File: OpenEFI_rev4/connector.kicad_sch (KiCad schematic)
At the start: 58 parts, among them J6 1241434-1, Q10 PMN30XPX, Q20 PMN30XPX, Q5 SS8050, Q6 IRLZ44N, Q7 IRLZ44N, U14 MIC5205-3.3YM5, U16 TPS5430DDA, U17 L78M05ABDT-TR, U4 AMS1117-3.3, U6 LT4363IMS

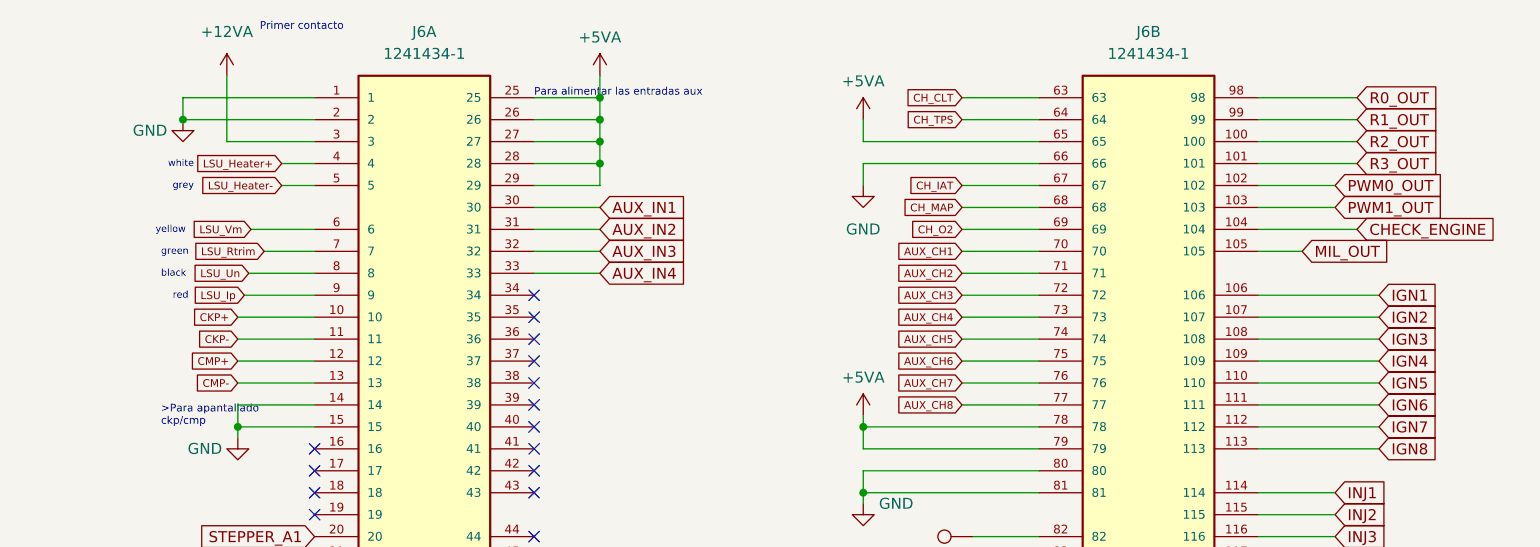
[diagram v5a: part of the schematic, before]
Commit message: fix board errors
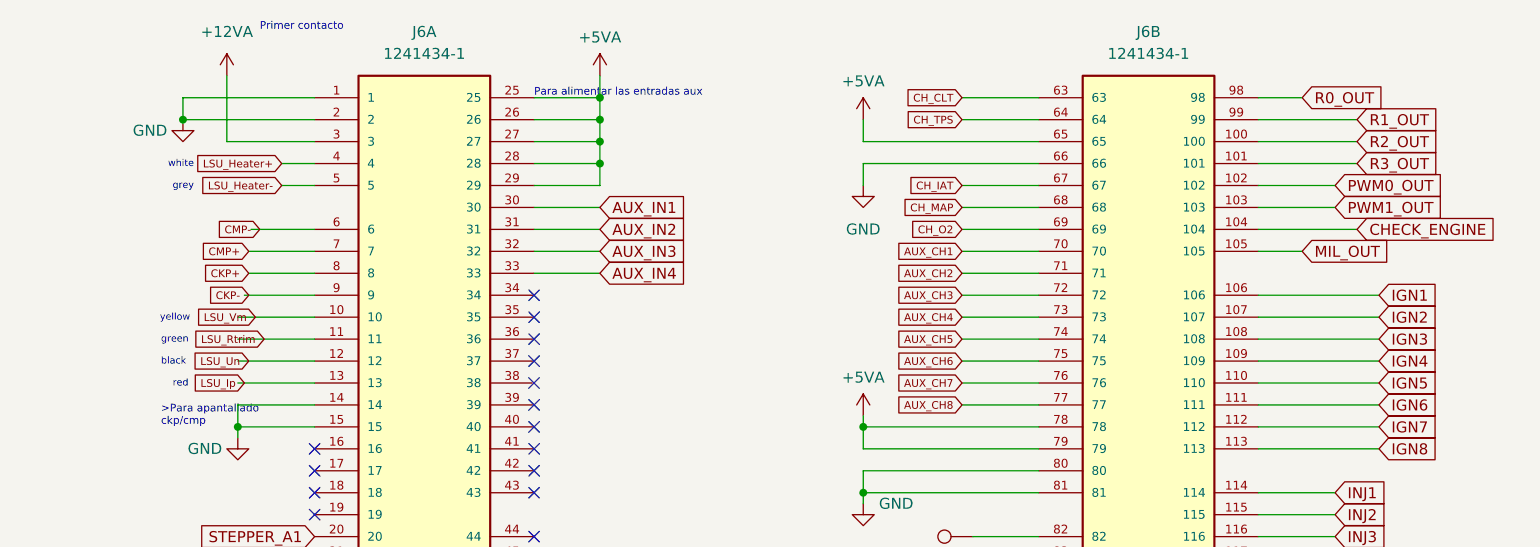
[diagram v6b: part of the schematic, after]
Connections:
- net CKP+: now also J6.8; no longer J6.10
- net CKP-: now also J6.9; no longer J6.11
- net CMP+: now also J6.7; no longer J6.12
- net CMP-: now also J6.6; no longer J6.13
- net LSU_Ip: now also J6.13; no longer J6.9
- net LSU_Rtrim: now also J6.11; no longer J6.7
- net LSU_Un: now also J6.12; no longer J6.8
- net LSU_Vm: now also J6.10; no longer J6.6
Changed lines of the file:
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@@
     (stroke (width 0) (type default))
   )
-  (wire (pts (xy 256.54 27.94) (xy 267.97 27.94))
+  (wire (pts (xy 256.54 27.94) (xy 261.62 27.94))
     (stroke (width 0) (type default))
   )
@@
     (stroke (width 0) (type default))
   )
-  (wire (pts (xy 141.478 45.72) (xy 147.32 45.72))
+  (wire (pts (xy 139.7 45.72) (xy 147.32 45.72))
     (stroke (width 0) (type default))
   )
@@
     (fill (type none))
   )
-  (text "yellow" (at 128.905 43.815 0)
+  (text "yellow" (at 129.413 53.975 0)
     (effects (font (size 0.8 0.8)) (justify left bottom))
   )
@@
     (effects (font (size 0.889 0.889)) (justify left bottom))
   )
-  (text "green" (at 129.54 46.355 0)
+  (text "green" (at 129.54 56.515 0)
     (effects (font (size 0.8 0.8)) (justify left bottom))
   )
@@
     (effects (font (size 0.8 0.8)) (justify right bottom))
   )
-  (text "black" (at 129.54 48.895 0)
+  (text "black" (at 129.54 59.055 0)
     (effects (font (size 0.8 0.8)) (justify left bottom))
   )
@@
     (effects (font (size 2 2)) (justify left bottom))
   )
-  (text "red" (at 132.715 51.435 0)
+  (text "red" (at 132.715 61.595 0)
     (effects (font (size 0.8 0.8)) (justify right bottom))
   )
@@
     )
   )
-  (global_label "LSU_Vm" (shape input) (at 139.954 43.18 180)
-    (effects (font (size 0.889 0.889)) (justify right))
-    (property "Intersheetrefs" "${INTERSHEET_REFS}" (at 136.5293 43.1245 0)
+  (global_label "LSU_Vm" (shape input) (at 140.462 53.34 180)
+    (effects (font (size 0.889 0.889)) (justify right))
+    (property "Intersheetrefs" "${INTERSHEET_REFS}" (at 137.0373 53.2845 0)
       (effects (font (size 0.889 0.889)) (justify right) hide)
     )
@@
     )
   )
-  (global_label "CKP-" (shape input) (at 138.43 55.88 180)
-    (effects (font (size 0.889 0.889)) (justify right))
-    (property "Intersheetrefs" "${INTERSHEET_REFS}" (at 132.9733 55.9355 0)
+  (global_label "CKP-" (shape input) (at 139.7 50.8 180)
+    (effects (font (size 0.889 0.889)) (justify right))
+    (property "Intersheetrefs" "${INTERSHEET_REFS}" (at 134.2433 50.8555 0)
       (effects (font (size 0.889 0.889)) (justify right) hide)
     )
@@
     )
   )
-  (global_label "R0_OUT" (shape input) (at 267.97 27.94 0)
-    (effects (font (size 1.27 1.27)) (justify left))
-    (property "Intersheetrefs" "${INTERSHEET_REFS}" (at 272.9231 27.8606 0)
+  (global_label "R0_OUT" (shape input) (at 261.62 27.94 0)
+    (effects (font (size 1.27 1.27)) (justify left))
+    (property "Intersheetrefs" "${INTERSHEET_REFS}" (at 266.5731 27.8606 0)
       (effects (font (size 1.27 1.27)) (justify left) hide)
     )
@@
     )
   )
-  (global_label "LSU_Un" (shape input) (at 139.7 48.26 180)
-    (effects (font (size 0.889 0.889)) (justify right))
-    (property "Intersheetrefs" "${INTERSHEET_REFS}" (at 136.2753 48.2045 0)
+  (global_label "LSU_Un" (shape input) (at 139.7 58.42 180)
+    (effects (font (size 0.889 0.889)) (justify right))
+    (property "Intersheetrefs" "${INTERSHEET_REFS}" (at 136.2753 58.3645 0)
       (effects (font (size 0.889 0.889)) (justify right) hide)
     )
@@
     )
   )
-  (global_label "LSU_Ip" (shape input) (at 139.192 50.8 180)
-    (effects (font (size 0.889 0.889)) (justify right))
-    (property "Intersheetrefs" "${INTERSHEET_REFS}" (at 135.7673 50.7445 0)
+  (global_label "LSU_Ip" (shape input) (at 139.192 60.96 180)
+    (effects (font (size 0.889 0.889)) (justify right))
+    (property "Intersheetrefs" "${INTERSHEET_REFS}" (at 135.7673 60.9045 0)
       (effects (font (size 0.889 0.889)) (justify right) hide)
     )
@@
     )
   )
-  (global_label "CKP+" (shape input) (at 138.43 53.34 180)
-    (effects (font (size 0.889 0.889)) (justify right))
-    (property "Intersheetrefs" "${INTERSHEET_REFS}" (at 132.9733 53.3955 0)
+  (global_label "CKP+" (shape input) (at 139.7 48.26 180)
+    (effects (font (size 0.889 0.889)) (justify right))
+    (property "Intersheetrefs" "${INTERSHEET_REFS}" (at 134.2433 48.3155 0)
       (effects (font (size 0.889 0.889)) (justify right) hide)
     )
@@
     )
   )
-  (global_label "CMP-" (shape input) (at 138.43 60.96 180)
-    (effects (font (size 0.889 0.889)) (justify right))
-    (property "Intersheetrefs" "${INTERSHEET_REFS}" (at 132.8463 61.0155 0)
+  (global_label "CMP-" (shape input) (at 140.97 43.18 180)
+    (effects (font (size 0.889 0.889)) (justify right))
+    (property "Intersheetrefs" "${INTERSHEET_REFS}" (at 135.3863 43.2355 0)
       (effects (font (size 0.889 0.889)) (justify right) hide)
     )
@@
     )
   )
-  (global_label "CMP+" (shape input) (at 138.43 58.42 180)
-    (effects (font (size 0.889 0.889)) (justify right))
-    (property "Intersheetrefs" "${INTERSHEET_REFS}" (at 132.8463 58.4755 0)
+  (global_label "CMP+" (shape input) (at 139.7 45.72 180)
+    (effects (font (size 0.889 0.889)) (justify right))
+    (property "Intersheetrefs" "${INTERSHEET_REFS}" (at 134.1163 45.7755 0)
       (effects (font (size 0.889 0.889)) (justify right) hide)
     )
@@
     )
   )
-  (global_label "LSU_Rtrim" (shape input) (at 141.478 45.72 180)
-    (effects (font (size 0.889 0.889)) (justify right))
-    (property "Intersheetrefs" "${INTERSHEET_REFS}" (at 138.0533 45.6645 0)
-      (effects (font (size 0.889 0.889)) (justify right) hide)
-    )
+  (global_label "LSU_Rtrim" (shape input) (at 141.478 55.88 180)
+    (effects (font (size 0.889 0.889)) (justify right))
+    (property "Intersheetrefs" "${INTERSHEET_REFS}" (at 138.0533 55.8245 0)
+      (effects (font (size 0.889 0.889)) (justify right) hide)
+    )

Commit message: wip SD card
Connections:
- net TACHO_OUT: now reaches J6.19
- no-connect marks 32 -> 31
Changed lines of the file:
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@@
   (no_connect (at 91.44 163.83))
   (no_connect (at 172.72 101.6))
-  (no_connect (at 147.32 76.2))
   (no_connect (at 172.72 55.88))
   (wire (pts (xy 222.25 58.42) (xy 231.14 58.42))
@@
     )
   )
+  (global_label "TACHO_OUT" (shape input) (at 147.32 76.2 180)
+    (effects (font (size 0.889 0.889)) (justify right))
+    (property "Intersheetrefs" "${INTERSHEET_REFS}" (at 144.0223 76.2555 0)
+      (effects (font (size 0.889 0.889)) (justify right) hide)
+    )
+  )

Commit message: WIP Rev4 SPI
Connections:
- net LSU_Un: now also J6.10; no longer J6.12
- net LSU_Vm: now also J6.12; no longer J6.10
- net STEPPER_A1: now also J6.21; no longer J6.20
- net STEPPER_A2: now also J6.20; no longer J6.21
